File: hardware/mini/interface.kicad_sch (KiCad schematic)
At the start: 41 parts, among them J4 FPC_12P_TOP_CONTACT, Q1 AO3400A, SW1 SKPMCAE030, SW2 SKPMCAE030, SW3 SKPMCAE030, SW4 SKPMCAE030, SW5 SKPMCAE030, SW6 SKPMCAE030, SW7 SKPMCAE030, SW8 SKPMCAE030, SW9 SKPMCAE030

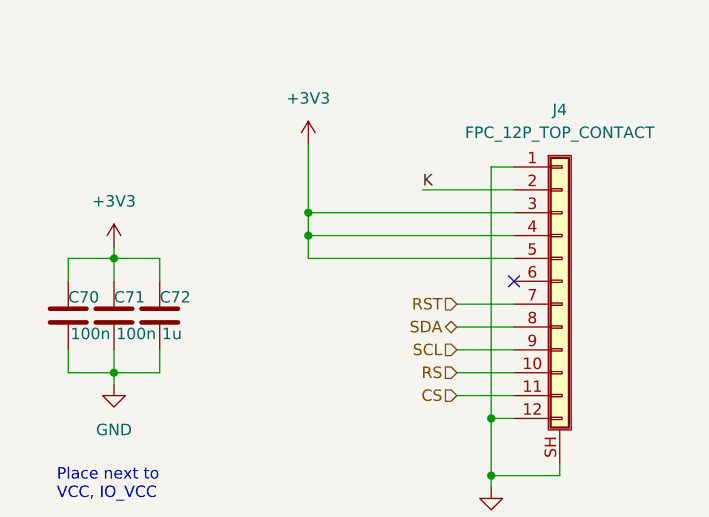
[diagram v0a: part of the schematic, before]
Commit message: reroute all except 3V3 & GND
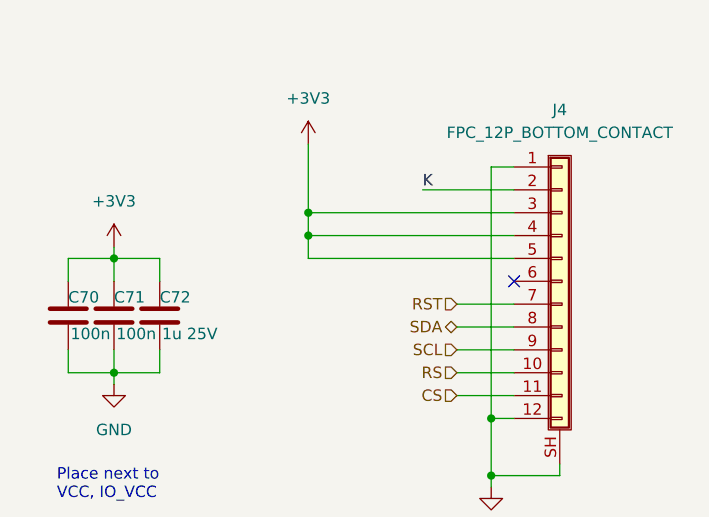
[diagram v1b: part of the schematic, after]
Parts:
- C72: value 1u -> 1u 25V; footprint Capacitor_SMD:C_0603_1608Metric -> Capacitor_SMD:C_0402_1005Metric; LCSC C15849 -> C52923
- J4: value FPC_12P_TOP_CONTACT -> FPC_12P_BOTTOM_CONTACT; LCSC C262585 -> C262559
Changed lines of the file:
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@@
 			)
 		)
-		(property "Value" "1u"
+		(property "Value" "1u 25V"
 			(at 226.314 75.6921 0)
 			(effects
@@
 			)
 		)
-		(property "Footprint" "Capacitor_SMD:C_0603_1608Metric"
+		(property "Footprint" "Capacitor_SMD:C_0402_1005Metric"
 			(at 227.0252 77.47 0)
 			(effects
@@
 			)
 		)
-		(property "LCSC" "C15849"
+		(property "LCSC" "C52923"
 			(at 226.06 73.66 0)
 			(effects
@@
 			)
 		)
-		(property "Value" "FPC_12P_TOP_CONTACT"
+		(property "Value" "FPC_12P_BOTTOM_CONTACT"
 			(at 270.51 53.34 0)
 			(effects
@@
 			)
 		)
-		(property "LCSC" "C262585"
+		(property "LCSC" "C262559"
 			(at 270.51 69.85 0)
 			(effects

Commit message: fix diode footprint
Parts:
- D10, D11, D12, D13, D14, D15, D4, D5, D6: footprint Diode_SMD:D_SOD-323 -> protovolt_mini_fp:D_SOD-323
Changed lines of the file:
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@@
 			)
 		)
-		(property "Footprint" "Diode_SMD:D_SOD-323"
+		(property "Footprint" "protovolt_mini_fp:D_SOD-323"
 			(at 189.23 123.19 0)
 			(effects
@@
 			)
 		)
-		(property "Footprint" "Diode_SMD:D_SOD-323"
+		(property "Footprint" "protovolt_mini_fp:D_SOD-323"
 			(at 148.59 104.14 0)
 			(effects
@@
 			)
 		)
-		(property "Footprint" "Diode_SMD:D_SOD-323"
+		(property "Footprint" "protovolt_mini_fp:D_SOD-323"
 			(at 189.23 104.14 0)
 			(effects
@@
 			)
 		)
-		(property "Footprint" "Diode_SMD:D_SOD-323"
+		(property "Footprint" "protovolt_mini_fp:D_SOD-323"
 			(at 168.91 85.09 0)
 			(effects
@@
 			)
 		)
-		(property "Footprint" "Diode_SMD:D_SOD-323"
+		(property "Footprint" "protovolt_mini_fp:D_SOD-323"
 			(at 148.59 85.09 0)
 			(effects
@@
 			)
 		)
-		(property "Footprint" "Diode_SMD:D_SOD-323"
+		(property "Footprint" "protovolt_mini_fp:D_SOD-323"
 			(at 148.59 123.19 0)
 			(effects
@@
 			)
 		)
-		(property "Footprint" "Diode_SMD:D_SOD-323"
+		(property "Footprint" "protovolt_mini_fp:D_SOD-323"
 			(at 189.23 85.09 0)
 			(effects
@@
 			)
 		)
-		(property "Footprint" "Diode_SMD:D_SOD-323"
+		(property "Footprint" "protovolt_mini_fp:D_SOD-323"
 			(at 168.91 123.19 0)
 			(effects
@@
 			)
 		)
-		(property "Footprint" "Diode_SMD:D_SOD-323"
+		(property "Footprint" "protovolt_mini_fp:D_SOD-323"
 			(at 168.91 104.14 0)
 			(effects

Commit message: cleanup schematic
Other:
- title: (none) -> Protovolt MINI
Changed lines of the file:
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@@
 	(generator_version "9.0")
 	(paper "A4")
+	(title_block
+		(title "Protovolt MINI")
+		(date "2025-06-16")
+		(rev "A")
+		(comment 3 "MINI")
+		(comment 4 "Protovolt")
+	)
 	(text "Place next to\nVCC, IO_VCC"
 		(exclude_from_sim no)

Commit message: first fab run
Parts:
- R40: value 5.1k -> 10k; LCSC C25905 -> C25744
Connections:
- net +3V3: now also J4.10 (Pin_10), J4.8 (Pin_8), J4.9 (Pin_9); no longer J4.3 (Pin_3), J4.4 (Pin_4), J4.5 (Pin_5)
- net CS: now also J4.2 (Pin_2); no longer J4.11 (Pin_11)
- net K: now also J4.11 (Pin_11); no longer J4.2 (Pin_2)
- net RS: now also J4.3 (Pin_3); no longer J4.10 (Pin_10)
- net RST: now also J4.6 (Pin_6); no longer J4.7 (Pin_7)
- net SCL: now also J4.4 (Pin_4); no longer J4.9 (Pin_9)
- net SDA: now also J4.5 (Pin_5); no longer J4.8 (Pin_8)
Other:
- moved on the sheet: J4
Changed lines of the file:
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@@
 	)
 	(junction
-		(at 72.39 83.82)
+		(at 270.51 52.07)
 		(diameter 0)
 		(color 0 0 0 0)
 	)
 	(junction
-		(at 220.98 80.01)
+		(at 72.39 83.82)
 		(diameter 0)
 		(color 0 0 0 0)
 	)
 	(junction
-		(at 177.8 95.25)
+		(at 220.98 80.01)
 		(diameter 0)
 		(color 0 0 0 0)
 	)
 	(junction
-		(at 48.26 119.38)
+		(at 177.8 95.25)
 		(diameter 0)
 		(color 0 0 0 0)
 	)
 	(junction
-		(at 262.89 85.09)
+		(at 48.26 119.38)
 		(diameter 0)
 		(color 0 0 0 0)
@@
 	(wire
 		(pts
+			(xy 259.08 74.93) (xy 265.43 74.93)
+		)
+		(stroke
+			(width 0)
+			(type default)
+		)
+	)
+	(wire
+		(pts
 			(xy 46.99 83.82) (xy 48.26 83.82)
 		)
@@
 	(wire
 		(pts
-			(xy 38.1 119.38) (xy 38.1 120.65)
+			(xy 274.32 52.07) (xy 274.32 91.44)
 		)
 		(stroke
@@
 	(wire
 		(pts
-			(xy 224.79 120.65) (xy 226.06 120.65)
+			(xy 38.1 119.38) (xy 38.1 120.65)
 		)
 		(stroke
@@
 	(wire
 		(pts
-			(xy 234.95 120.65) (xy 234.95 127)
+			(xy 224.79 120.65) (xy 226.06 120.65)
 		)
 		(stroke
@@
 	(wire
 		(pts
-			(xy 245.11 127) (xy 245.11 128.27)
+			(xy 234.95 120.65) (xy 234.95 127)
 		)
 		(stroke
@@
 	(wire
 		(pts
-			(xy 62.23 83.82) (xy 62.23 85.09)
+			(xy 245.11 127) (xy 245.11 128.27)
 		)
 		(stroke
@@
 	(wire
 		(pts
-			(xy 177.8 95.25) (xy 176.53 96.52)
+			(xy 62.23 83.82) (xy 62.23 85.09)
 		)
 		(stroke
@@
 	(wire
 		(pts
-			(xy 259.08 74.93) (xy 265.43 74.93)
+			(xy 177.8 95.25) (xy 176.53 96.52)
 		)
 		(stroke
@@
 	(wire
 		(pts
+			(xy 262.89 57.15) (xy 262.89 52.07)
+		)
+		(stroke
+			(width 0)
+			(type default)
+		)
+	)
+	(wire
+		(pts
 			(xy 38.1 48.26) (xy 38.1 49.53)
 		)
@@
 	(wire
 		(pts
+			(xy 270.51 52.07) (xy 274.32 52.07)
+		)
+		(stroke
+			(width 0)
+			(type default)
+		)
+	)
+	(wire
+		(pts
 			(xy 157.48 76.2) (xy 157.48 95.25)
 		)
@@
 	(wire
 		(pts
+			(xy 262.89 52.07) (xy 270.51 52.07)
+		)
+		(stroke
+			(width 0)
+			(type default)
+		)
+	)
+	(wire
+		(pts
 			(xy 30.48 74.93) (xy 30.48 92.71)
 		)
@@
 	(wire
 		(pts
-			(xy 270.51 91.44) (xy 270.51 90.17)
-		)
-		(stroke
-			(width 0)
-			(type default)
-		)
-	)
-	(wire
-		(pts
 			(xy 234.95 120.65) (xy 237.49 120.65)
 		)
@@
 	(wire
 		(pts
-			(xy 262.89 57.15) (xy 262.89 85.09)
-		)
-		(stroke
-			(width 0)
-			(type default)
-		)
-	)
-	(wire
-		(pts
 			(xy 257.81 111.76) (xy 262.89 111.76)
 		)
@@
 	(wire
 		(pts
-			(xy 262.89 91.44) (xy 270.51 91.44)
+			(xy 262.89 91.44) (xy 274.32 91.44)
 		)
 		(stroke
@@
 	(symbol
 		(lib_id "Connector_Generic_Shielded:Conn_01x12_Shielded")
-		(at 270.51 69.85 0)
+		(at 270.51 72.39 0)
+		(mirror x)
 		(unit 1)
 		(exclude_from_sim no)
@@
 		(dnp no)
 		(property "Reference" "J4"
-			(at 270.51 50.8 0)
+			(at 288.036 92.202 0)
 			(effects
 				(font
@@
 		)
 		(property "Value" "FPC_12P_BOTTOM_CONTACT"
-			(at 270.51 53.34 0)
+			(at 288.036 89.662 0)
 			(effects
 				(font
@@
 		)
 		(property "Footprint" "protovolt_mini_fp:JUSHUO_AFC07-S12ECA-00_1x12-1MP_P0.5mm_Horizontal"
-			(at 270.51 69.85 0)
+			(at 270.51 72.39 0)
 			(effects
 				(font
@@
 		)
 		(property "Datasheet" "~"
-			(at 270.51 69.85 0)
+			(at 270.51 72.39 0)
 			(effects
 				(font
@@
 		)
 		(property "Description" "Generic shielded connector, single row, 01x12, script generated (kicad-library-utils/schlib/autogen/connector/)"
-			(at 270.51 69.85 0)
+			(at 270.51 72.39 0)
 			(effects
 				(font
@@
 		)
 		(property "LCSC" "C262559"
-			(at 270.51 69.85 0)
+			(at 270.51 72.39 0)
 			(effects
 				(font
@@
 			)
 		)
-		(property "Value" "5.1k"
+		(property "Value" "10k"
 			(at 229.362 126.238 90)
 			(effects
@@
 			)
 		)
-		(property "LCSC" "C25905"
+		(property "LCSC" "C25744"
 			(at 240.03 127 0)
 			(effects
